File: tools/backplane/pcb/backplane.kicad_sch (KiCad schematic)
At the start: 0 parts

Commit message: start adding connectors to the backplane
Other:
- added sheet Card0 (schematics/card0.kicad_sch)
- added sheet Card1 (schematics/card1.kicad_sch)
- added sheet Card2 (schematics/card2.kicad_sch)
- added sheet Card3 (schematics/card3.kicad_sch)
- added sheet Card4 (schematics/card4.kicad_sch)
- added sheet Card5 (schematics/card5.kicad_sch)
- added sheet Card6 (schematics/card6.kicad_sch)
- added sheet Card7 (schematics/card7.kicad_sch)
- added sheet Card8 (schematics/card8.kicad_sch)
- added sheet Card9 (schematics/card9.kicad_sch)

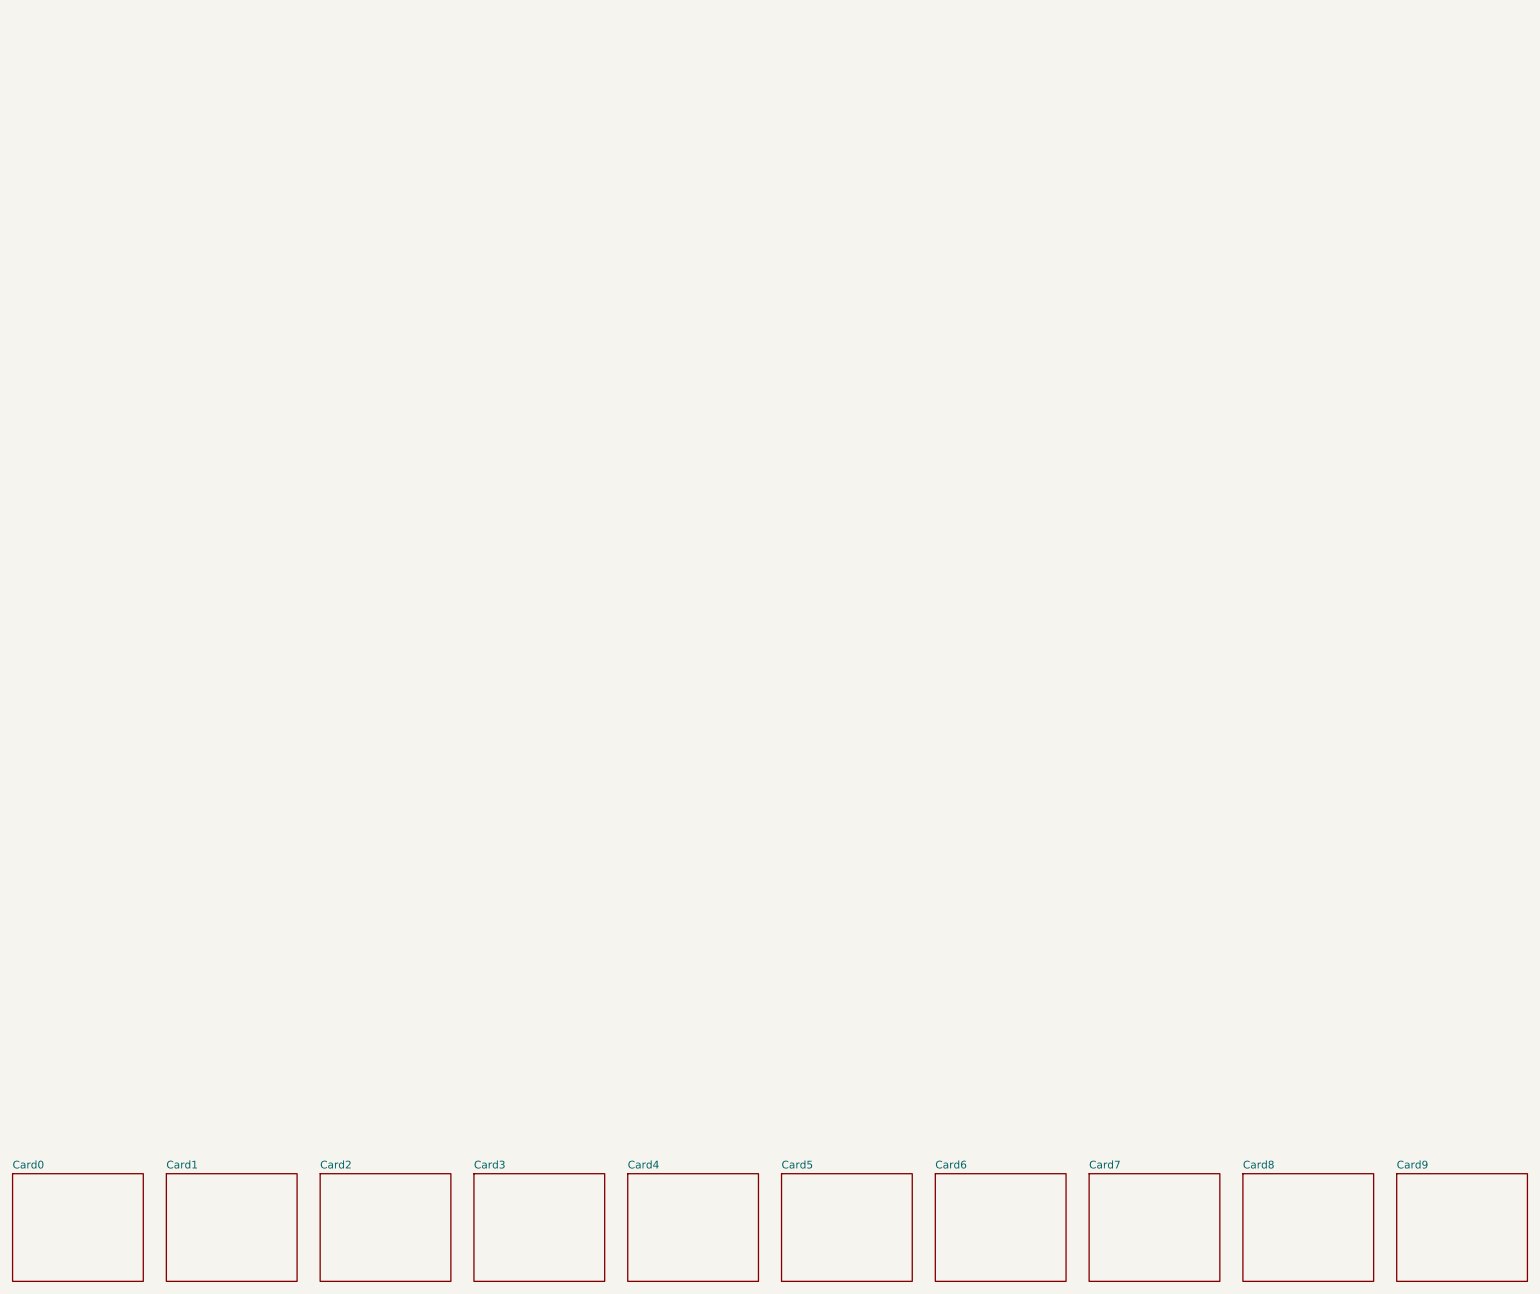
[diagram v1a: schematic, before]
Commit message: start routing the backplane
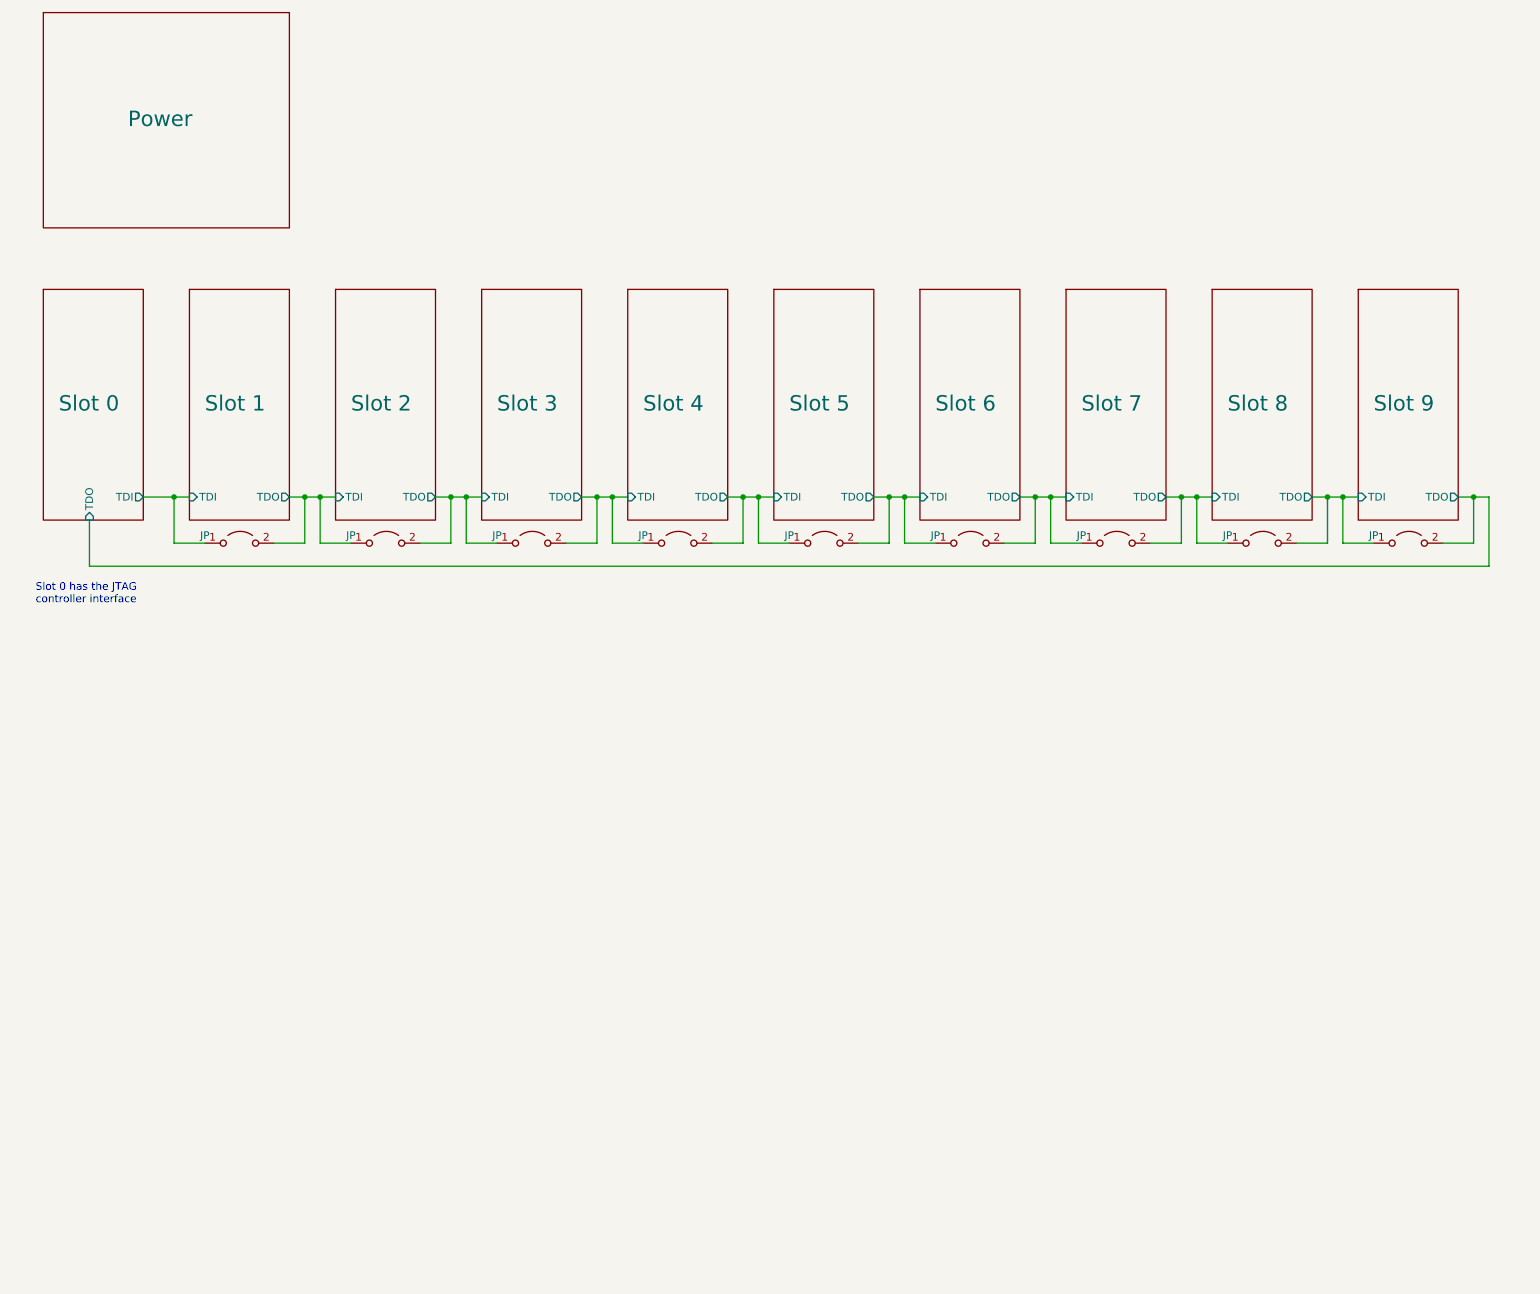
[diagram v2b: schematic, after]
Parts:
- added JP (x9): Jumper_2_Open, symbol Jumper:Jumper_2_Open
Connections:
- new net Slot 0/TDI: JP.1 (A)
- new net Slot 0/TDO: JP.2 (B)
- new net Slot 1/TDO: JP.1 (A), JP.2 (B)
- new net Slot 2/TDO: JP.1 (A), JP.2 (B)
- new net Slot 3/TDO: JP.1 (A), JP.2 (B)
- new net Slot 4/TDO: JP.1 (A), JP.2 (B)
- new net Slot 5/TDO: JP.1 (A), JP.2 (B)
- new net Slot 6/TDO: JP.1 (A), JP.2 (B)
- new net Slot 7/TDO: JP.1 (A), JP.2 (B)
- new net Slot 8/TDO: JP.1 (A), JP.2 (B)
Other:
- sheet Card0 renamed Slot 0
- sheet Card1 renamed Slot 1
- sheet Card2 renamed Slot 2
- sheet Card3 renamed Slot 3
- sheet Card4 renamed Slot 4
- sheet Card5 renamed Slot 5
- sheet Card6 renamed Slot 6
- sheet Card7 renamed Slot 7
- sheet Card8 renamed Slot 8
- sheet Card9 renamed Slot 9
- added sheet Power (schematics/power.kicad_sch)
- sheet Slot 0 ports: added TDI, TDO; removed none
- sheet Slot 1 ports: added TDI, TDO; removed none
- sheet Slot 2 ports: added TDI, TDO; removed none
- sheet Slot 3 ports: added TDI, TDO; removed none
- sheet Slot 4 ports: added TDI, TDO; removed none
- sheet Slot 5 ports: added TDI, TDO; removed none
- sheet Slot 6 ports: added TDI, TDO; removed none
- sheet Slot 7 ports: added TDI, TDO; removed none
- sheet Slot 8 ports: added TDI, TDO; removed none
- sheet Slot 9 ports: added TDI, TDO; removed none
- note added: "Slot 0 has the JTAG controller interface"
